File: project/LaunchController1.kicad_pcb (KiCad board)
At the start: 2 copper layers, 99.1 x 80 mm, 26 parts, among them J1 691137710002, J2 CB2B-XH-AM, J3 B2B-XH-AM, Q1 BJT_PNP, Q2 BJT_PNP, SW1 ANT11SF1CQE, SW2 D6R40F2LFS

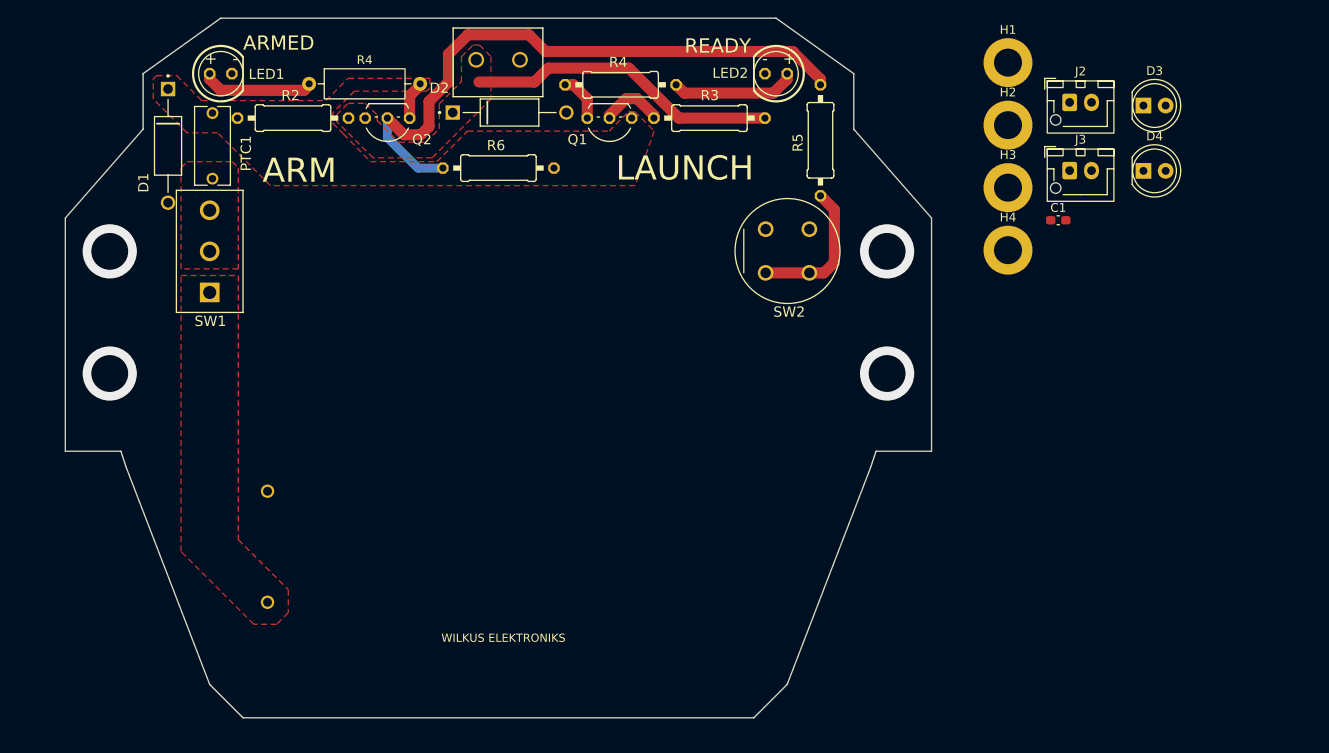
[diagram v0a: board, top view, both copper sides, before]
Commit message: Feat: increased PTC current rating, dropped R5 to ensure saturation on Q2
Also switched all parts (except the battery case) to a KiCad library part to update. Moving the design to KiCad (r.i.p Eagle).

Increased current rating of PTC1 to 2.5A hold, 5A trip to reduce possibility of inadvertent tripping.
Dropped R5 to ensure saturation on Q2
Q2 is surprisingly able to handle the pulse current. Peak pulse is 6A, which should cover requirement. Maybe consider ZTX618 instead, which has a higher amp rating.
Q2 (ZTX718) is being retired, so if you're reading this you need to pick a different part.
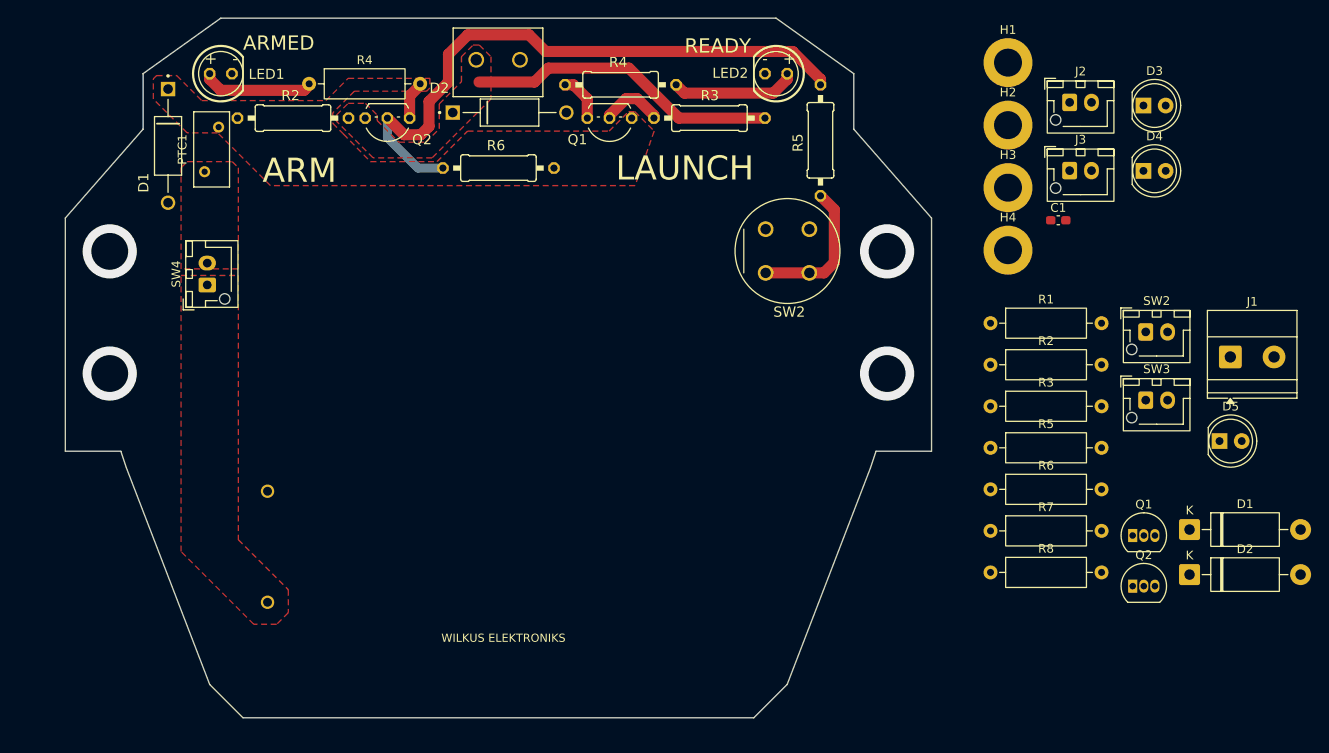
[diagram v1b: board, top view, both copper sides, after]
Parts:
- removed SW1: ANT11SF1CQE, ANT11SF1CQE
- added D1: P6KE7.5CA/B, Diode_THT:D_DO-15_P12.70mm_Horizontal, F.Cu at (227.5, 123.5)
- added D2: P6KE7.5CA/B, Diode_THT:D_DO-15_P12.70mm_Horizontal, F.Cu at (227.5, 128.6)
- added D5: LED, LED_THT:LED_D5.0mm, F.Cu at (231.0, 113.4)
- added J1: 1729128, TerminalBlock_Phoenix:TerminalBlock_Phoenix_MKDS-1,5-2_1x02_P5.00mm_Horizontal, F.Cu at (232.2, 103.7)
- added Q1: ZTX718, Package_TO_SOT_THT:TO-92_Inline, F.Cu at (221.0, 124.2)
- added Q2: ZTX718, Package_TO_SOT_THT:TO-92_Inline, F.Cu at (221.0, 130.0)
- added R1: 300, Resistor_THT:R_Axial_DIN0309_L9.0mm_D3.2mm_P12.70mm_Horizontal, F.Cu at (204.8, 99.9)
- added R2: 4.7K, Resistor_THT:R_Axial_DIN0309_L9.0mm_D3.2mm_P12.70mm_Horizontal, F.Cu at (204.8, 104.6)
- added R3: 4.7K, Resistor_THT:R_Axial_DIN0309_L9.0mm_D3.2mm_P12.70mm_Horizontal, F.Cu at (204.8, 109.4)
- added R5: 300, Resistor_THT:R_Axial_DIN0309_L9.0mm_D3.2mm_P12.70mm_Horizontal, F.Cu at (204.8, 114.1)
- added R6: 4.7K, Resistor_THT:R_Axial_DIN0309_L9.0mm_D3.2mm_P12.70mm_Horizontal, F.Cu at (204.8, 118.9)
- added R7: 300, Resistor_THT:R_Axial_DIN0309_L9.0mm_D3.2mm_P12.70mm_Horizontal, F.Cu at (204.8, 123.6)
- added R8: 10K, Resistor_THT:R_Axial_DIN0309_L9.0mm_D3.2mm_P12.70mm_Horizontal, F.Cu at (204.8, 128.4)
- added SW2: B2B-XH-AM, Connector_JST:JST_XH_B2B-XH-AM_1x02_P2.50mm_Vertical, F.Cu at (222.5, 100.9)
- added SW3: B2B-XH-AM, Connector_JST:JST_XH_B2B-XH-AM_1x02_P2.50mm_Vertical, F.Cu at (222.5, 108.7)
- added SW4: B2B-XH-AM, Connector_JST:JST_XH_B2B-XH-AM_1x02_P2.50mm_Vertical, F.Cu at (115.2, 95.5)
- PTC1: value 0ZRG0120FF2E -> 0ZRG0250FF1E; footprint 0ZRG -> Fuse:Fuse_BelFuse_0ZRE0012FF_L8.3mm_W3.8mm
- moved PTC1 3.09 mm to (114.9, 82.6)
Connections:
- C1 pad 1: Net-(J2-Pin_1) -> /launch
- D3 pad 1: Net-(BT1-NEG) -> GND
- D4 pad 1: Net-(BT1-NEG) -> GND
- PTC1 pad 2: N$10 -> /safed_power
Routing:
- added copper zone on F.Cu, net N$2
- removed copper zone on F.Cu, net Net-(SW4-B)

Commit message: layout: Updated layout for schematic
Rev -
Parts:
- removed BT1: 6V, BAT_2477
- removed the D1 at (110.7, 79.6)
- removed the D2 at (149.8, 75.8)
- removed the J1 at (146.0, 69.8)
- removed LED1, LED2: , LED5MM
- removed the Q1 at (161.2, 76.4)
- removed the Q2 at (221.0, 130.0)
- removed the Q2 at (135.8, 76.4)
- removed the R2 at (125.0, 76.4)
- removed the R3 at (172.6, 76.4)
- removed the R4 at (126.9, 72.5)
- removed the R4 at (162.5, 72.6)
- removed R5: 300, Resistor_THT:R_Axial_DIN0309_L9.0mm_D3.2mm_P12.70mm_Horizontal
- removed R5: 300, 0309_12
- removed the R6 at (148.5, 82.1)
- removed the SW2 at (184.1, 89.1)
- added G***: LOGO, JM-Library:lotus_moon, B.Cu at (117.7, 141.0)
- added Q2: AOD413A, Package_TO_SOT_SMD:TO-252-3_TabPin2, F.Cu at (136.0, 102.5)
- added R4: 300, Resistor_THT:R_Axial_DIN0309_L9.0mm_D3.2mm_P12.70mm_Horizontal, F.Cu at (115.8, 86.5)
- added R9: 60, Resistor_THT:R_Axial_DIN0309_L9.0mm_D3.2mm_P12.70mm_Horizontal, F.Cu at (100.2, 100.0)
- added REF**: OSHW-Logo2_7.3x6mm_SilkScreen, Symbol:OSHW-Logo2_7.3x6mm_SilkScreen, B.Cu at (110.7, 141.0)
- added TP1: TestPoint, TestPoint:TestPoint_Pad_2.0x2.0mm, F.Cu at (120.0, 116.5)
- D1, D2: value P6KE7.5CA/B -> P6KE7.5A/B
- J2: value CB2B-XH-AM -> XT30PW-M; footprint Connector_JST:JST_XH_B2B-XH-AM_1x02_P2.50mm_Vertical -> Connector_AMASS:AMASS_XT30PW-M_1x02_P2.50mm_Horizontal
- moved D5 131.0 mm to (100.5, 125.0)
- moved H1 126.1 mm to (102.5, 141.0)
- moved SW3 120.5 mm to (102.0, 106.5)
- moved SW2 119.1 mm to (104.5, 117.0), turned to 180 degrees
- moved D4 116.9 mm to (105.8, 92.5), turned to 180 degrees
- moved D1 114.2 mm to (114.0, 135.5), turned to 180 degrees
- moved Q1 111.4 mm to (114.2, 92.5)
- moved H2 104.3 mm to (102.5, 77.0)
- moved J1 103.1 mm to (132.0, 79.3), turned to 180 degrees
- moved J2 100.6 mm to (131.5, 132.5), turned to -90 degrees
- moved D2 98.3 mm to (137.3, 89.5), turned to 180 degrees
- moved D3 97.6 mm to (133.0, 114.5), turned to 180 degrees
- moved R7 96.6 mm to (108.2, 125.0)
- moved R6 92.3 mm to (112.5, 116.3), turned to 90 degrees
- moved R8 91.5 mm to (113.3, 131.0), turned to 180 degrees
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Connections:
- D1 pad 1: (no net) -> /safed_power
- D1 pad 2: (no net) -> GND
- D2 pad 1: (no net) -> /igniter_hot
- D2 pad 2: (no net) -> GND
- J2 pad 1: Net-(J2-Pin_1) -> /battery
- J2 pad 2: Net-(J2-Pin_2) -> GND
- J3 pad 1: Net-(J2-Pin_2) -> /battery
- R6 pad 2: Net-(Q2-B) -> /launch
- SW3 pad 2: /launch -> Net-(SW3-B)
- SW4 pad 1: /pwr -> /battery
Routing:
- net /safed_power: track 0.00 -> 85.9 mm
- net N$3: track 71.3 -> 0.00 mm
- net /igniter_hot: track 0.00 -> 49.7 mm, vias 0 -> 14
- net IGNTR_HOT: track 35.7 -> 0.00 mm
- net /battery: track 0.00 -> 33.6 mm
- net /arm: track 0.00 -> 25.2 mm
- net /launch: track 0.00 -> 23.0 mm, vias 0 -> 2
- net N$8: track 16.6 -> 0.00 mm
- net N$11: track 14.4 -> 0.00 mm
- net N$5: track 12.9 -> 0.00 mm
- net Net-(SW3-B): track 0.00 -> 10.3 mm
- net N$1: track 7.29 -> 0.00 mm
- net Net-(SW4-B): track 0.00 -> 7.06 mm
- net Net-(Q1-C): track 0.00 -> 6.14 mm
- net Net-(D4-A): track 0.00 -> 6.04 mm
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- added copper zone on B.Cu, net /igniter_hot
- added copper zone on F.Cu, net /igniter_hot
- added copper zone on F.Cu, net /safed_power
- added copper zone on B.Cu, net GND
- removed copper zone on F.Cu, net IGNTR_HOT
- removed copper zone on F.Cu, net N$10
- removed copper zone on F.Cu, net N$2
- removed copper zone on F.Cu, net PWR
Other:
- board size 99.1 x 80 mm -> 46.5 x 71.5 mm
- board text added: "+"
- board text added: "-"
- board text added: "MR-Launch-Controller Rev - 2026-08-06"
- board text added: "Model Rocket Launch Controller"
- board text removed: "+ -"
- board text removed: "- +"
- board text removed: "ARM"
- board text removed: "ARMED"
- board text removed: "LAUNCH"
- board text removed: "READY"
- board text removed: "WILKUS ELEKTRONIKS"
